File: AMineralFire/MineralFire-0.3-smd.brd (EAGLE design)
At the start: 109.9 x 77 mm, 86 parts, among them IC1 LM358, Q1 20MHz, Q2 20MHz, Q3 2N3906, Q4 2N3906, Q5 2N3906, Q6 2N3906, Q7 2N3906, Q8 2N3906, Q9 2N3906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

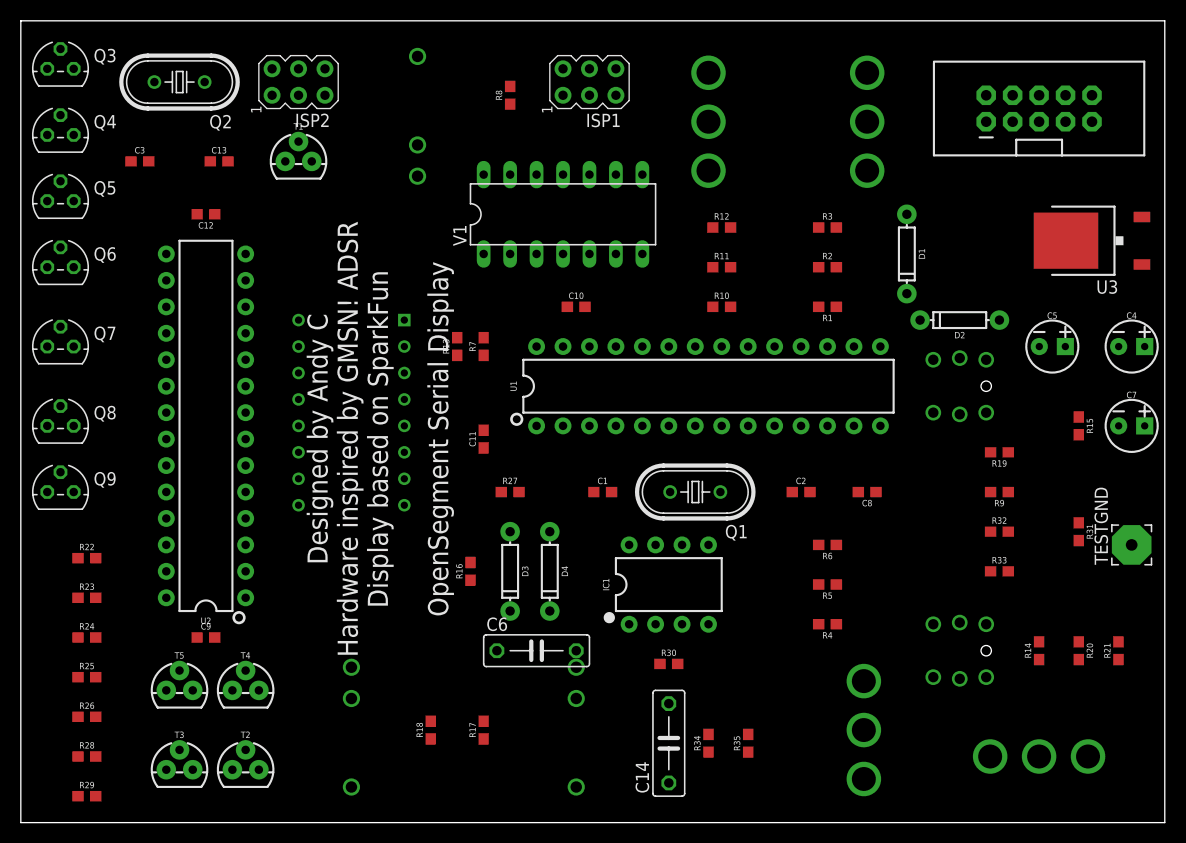
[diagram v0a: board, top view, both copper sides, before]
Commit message: Updated to almost all SMD
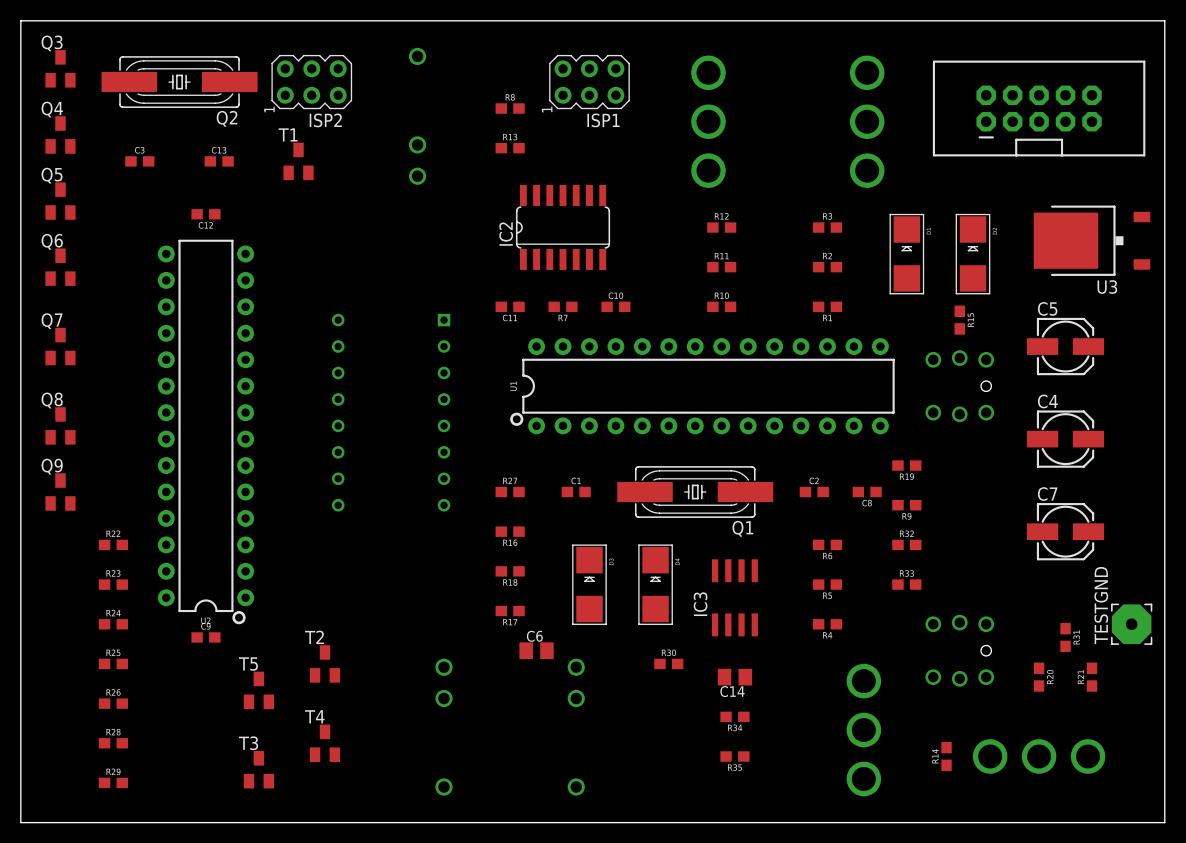
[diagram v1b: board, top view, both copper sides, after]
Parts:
- removed IC1: LM358, SparkFun-IC-Amplifiers:DIP08
- removed V1: 7409N, 74ttl-din:DIL14
- added IC2: 74LS09D, 74xx-eu:SO14
- added IC3: LM358D, linear:SO08
- C14, C6: device rcl:C075-032X103 -> rcl:C0805K
- C4, C5, C7: device SparkFun-Capacitors:CPOL-RADIAL-2.5MM-5MM -> rcl:153CLV-0505
- D1, D2, D3, D4: device SparkFun-DiscreteSemi:DIODE-1N4148 -> adafruit:SMADIODE
- Q1, Q2: device adafruit:HC49U70 -> adafruit:HC49UP
- Q3, Q4, Q5, Q6, Q7, Q8, Q9: value 2N3906 -> MMBT3906LT1SMD; device transistor-pnp:TO92 -> transistor-pnp:SOT23-BEC
- T1, T2, T3, T4, T5: device SparkFun-DiscreteSemi:TO-92 -> transistor:SOT23-BEC
- moved R13 19.7 mm to (47.0, 64.8), turned to 0 degrees
- moved R18 17.0 mm to (47.0, 24.1), turned to 180 degrees
- moved R15 15.3 mm to (90.2, 48.3)
- moved R14 13.5 mm to (88.9, 6.35)
- moved C11 13.0 mm to (47.0, 49.5), turned to 180 degrees
- moved T2 12.7 mm to (29.2, 15.2)
- moved C7 12.0 mm to (100.3, 27.9)
- moved R17 11.7 mm to (47.0, 20.3), turned to 180 degrees
- moved C4 10.9 mm to (100.3, 36.8)
- moved D4 10.2 mm to (61.0, 22.9)
- moved R31 10.2 mm to (100.3, 17.8)
- moved T4 9.16 mm to (29.2, 7.62)
- moved C14 8.98 mm to (68.6, 14.0), turned to 180 degrees
- moved R19 8.98 mm to (85.1, 34.3)
- moved R32 8.98 mm to (85.1, 26.7)
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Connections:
- net +12V: now also C4.+; no longer C4.1, IC1.8
- net +5V: now also C7.+, IC2.14, IC3.8, Q3.E, Q4.E, Q5.E, Q6.E, Q7.E, Q8.E, Q9.E; no longer C7.1, Q3.3, Q4.3, Q5.3, Q6.3, Q7.3, Q8.3, Q9.3, V1.14
- net -12V: now also C5.-; no longer C5.2
- net BUTLED: now also IC3.6; no longer IC1.5
- net C-DIG1: now also T2.B; no longer T2.2
- net C-DIG2: now also T3.B; no longer T3.2
- net C-DIG3: now also T4.B; no longer T4.2
- net C-DIG4: now also T5.B; no longer T5.2
- net C-SEGA: now also Q5.B; no longer Q5.2
- net C-SEGB: now also Q9.B; no longer Q9.2
- net C-SEGC: now also Q7.B; no longer Q7.2
- net C-SEGD: now also Q3.B; no longer Q3.2
- net C-SEGE: now also Q4.B; no longer Q4.2
- net C-SEGF: now also Q8.B; no longer Q8.2
- net C-SEGG: now also Q6.B; no longer Q6.2
- net D1: now also T2.C; no longer T2.3
- net D2: now also T3.C; no longer T3.3
- net D3: now also T4.C; no longer T4.3
- net D4: now also T5.C; no longer T5.3
- net GND: now also C4.-, C5.+, C7.-, IC2.7, IC3.4, T1.E, T2.E, T3.E, T4.E, T5.E; no longer C4.2, C5.1, C7.2, IC1.4, T1.1, T2.1, T3.1, T4.1, T5.1, V1.7
- net LBUTTON: now also IC2.2; no longer V1.2
- net LTRIG: now also IC2.1, T1.C; no longer T1.3, V1.1
- net N$11: now also Q3.C; no longer Q3.1
- net N$13: now also Q9.C; no longer Q9.1
- net N$14: now also Q8.C; no longer Q8.1
- net N$15: now also T1.B; no longer T1.2
- net N$16: now also Q7.C; no longer Q7.1
- net N$17: now also Q6.C; no longer Q6.1
- net N$19: now also IC3.7; no longer IC1.7
- net N$20: now also Q5.C; no longer Q5.1
- net N$24: now also IC3.5; no longer IC1.6
- net N$32: now also IC3.3; no longer IC1.2
- net N$33: now also IC3.1; no longer IC1.1
- net N$5: now also Q4.C; no longer Q4.1
- net TRIG: now also IC2.3; no longer V1.3
- net TRIGO: now also IC3.2; no longer IC1.3
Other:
- board text added: "V0.3 SMD"
- board text removed: "V0.3"
